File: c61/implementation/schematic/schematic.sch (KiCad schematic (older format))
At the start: 0 parts

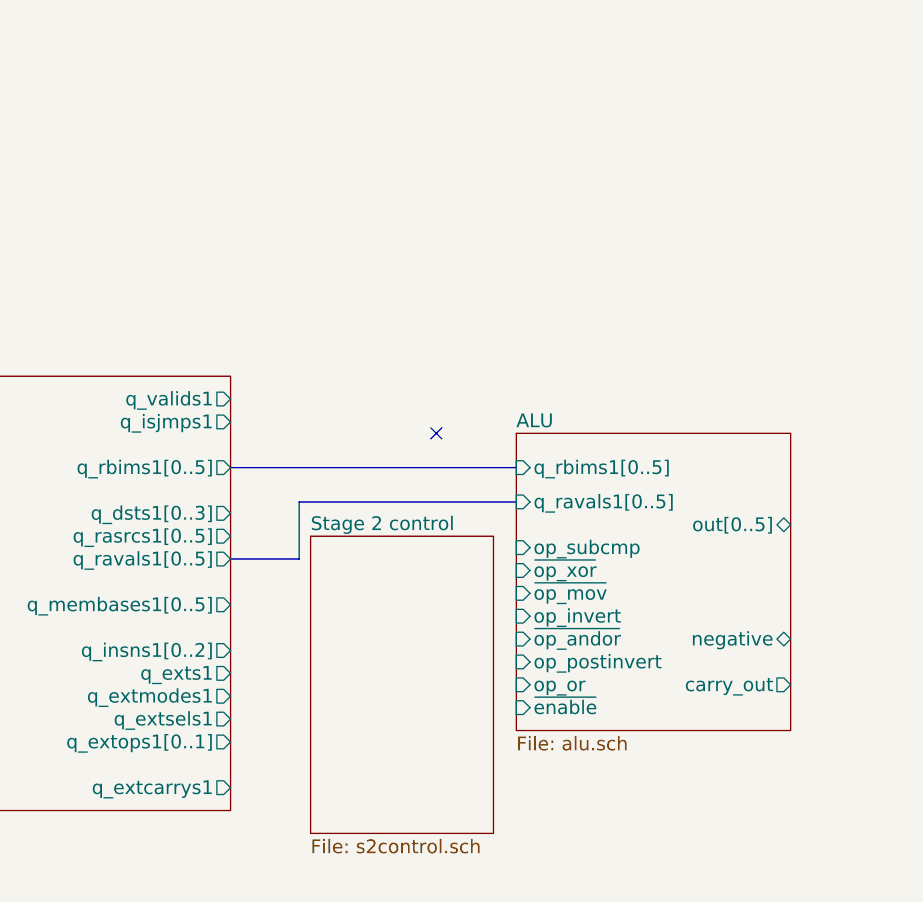
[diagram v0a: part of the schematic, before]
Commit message: C61: more updates to schematic
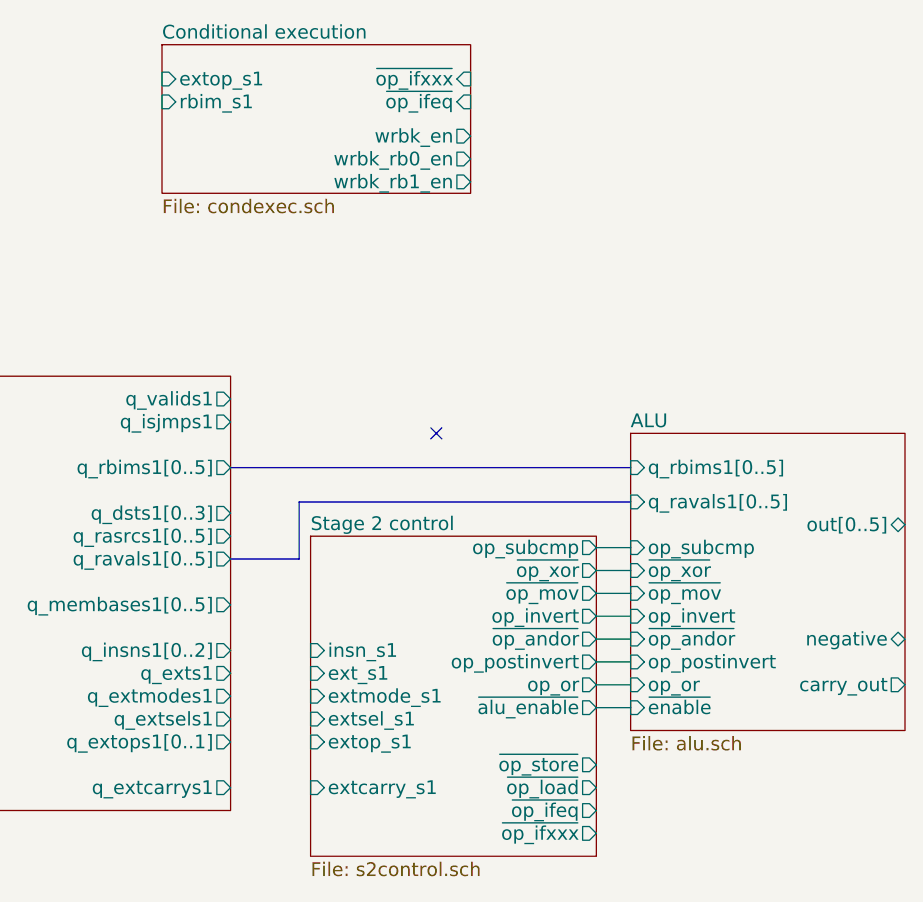
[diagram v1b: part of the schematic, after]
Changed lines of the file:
@@
 $Descr A4 11693 8268
 encoding utf-8
-Sheet 1 8
+Sheet 1 9
 Title ""
 Date ""
@@
 Connection ~ 2500 2350
 $Sheet
-S 9200 2500 1200 1300
+S 9700 2500 1200 1300
 U 5B67573A
 F0 "ALU" 60
 F1 "alu.sch" 60
-F2 "q_rbims1[0..5]" I L 9200 2650 60
-F3 "q_ravals1[0..5]" I L 9200 2800 60
-F4 "op_subcmp" I L 9200 3000 60
-F5 "~op_xor" I L 9200 3100 60
-F6 "~op_mov" I L 9200 3200 60
-F7 "op_invert" I L 9200 3300 60
-F8 "~op_andor" I L 9200 3400 60
-F9 "op_postinvert" I L 9200 3500 60
-F10 "op_or" I L 9200 3600 60
-F11 "~enable" I L 9200 3700 60
-F12 "out[0..5]" T R 10400 2900 60
-F13 "negative" T R 10400 3400 60
-F14 "carry_out" O R 10400 3600 60
-$EndSheet
-$Sheet
-S 8300 2950 800  1300
+F2 "q_rbims1[0..5]" I L 9700 2650 60
+F3 "q_ravals1[0..5]" I L 9700 2800 60
+F4 "op_subcmp" I L 9700 3000 60
+F5 "~op_xor" I L 9700 3100 60
+F6 "~op_mov" I L 9700 3200 60
+F7 "op_invert" I L 9700 3300 60
+F8 "~op_andor" I L 9700 3400 60
+F9 "op_postinvert" I L 9700 3500 60
+F10 "op_or" I L 9700 3600 60
+F11 "~enable" I L 9700 3700 60
+F12 "out[0..5]" T R 10900 2900 60
+F13 "negative" T R 10900 3400 60
+F14 "carry_out" O R 10900 3600 60
+$EndSheet
+$Sheet
+S 8300 2950 1250 1400
 U 5B6757FA
 F0 "Stage 2 control" 60
 F1 "s2control.sch" 60
+F2 "insn_s1" I L 8300 3450 60
+F3 "ext_s1" I L 8300 3550 60
+F4 "extmode_s1" I L 8300 3650 60
+F5 "extsel_s1" I L 8300 3750 60
+F6 "extop_s1" I L 8300 3850 60
+F7 "extcarry_s1" I L 8300 4050 60
+F8 "op_subcmp" O R 9550 3000 60
+F9 "~op_xor" O R 9550 3100 60
+F10 "~op_mov" O R 9550 3200 60
+F11 "~op_andor" O R 9550 3400 60
+F12 "op_invert" O R 9550 3300 60
+F13 "op_or" O R 9550 3600 60
+F14 "op_postinvert" O R 9550 3500 60
+F15 "~alu_enable" O R 9550 3700 60
+F16 "~op_store" O R 9550 3950 60
+F17 "~op_load" O R 9550 4050 60
+F18 "~op_ifeq" O R 9550 4150 60
+F19 "~op_ifxxx" O R 9550 4250 60
 $EndSheet
 Wire Bus Line
@@
 	8250 3050 8250 2800
 Wire Bus Line
-	8250 2800 9200 2800
-Wire Bus Line
-	7950 2650 9200 2650
+	8250 2800 9700 2800
+Wire Bus Line
+	7950 2650 9700 2650
 NoConn ~ 8850 2500
+Wire Wire Line
+	9550 3000 9700 3000
+Wire Wire Line
+	9550 3100 9700 3100
+Wire Wire Line
+	9550 3200 9700 3200
+Wire Wire Line
+	9550 3300 9700 3300
+Wire Wire Line
+	9550 3400 9700 3400
+Wire Wire Line
+	9550 3500 9700 3500
+Wire Wire Line
+	9550 3600 9700 3600
+Wire Wire Line
+	9550 3700 9700 3700
+$Sheet
+S 7650 800  1350 650
+U 5B95BAE6
+F0 "Conditional execution" 60
+F1 "condexec.sch" 60
+F2 "~op_ifeq" I R 9000 1050 60
+F3 "~op_ifxxx" I R 9000 950 60
+F4 "extop_s1" I L 7650 950 60
+F5 "rbim_s1" I L 7650 1050 60
+F6 "wrbk_en" O R 9000 1200 60
+F7 "wrbk_rb0_en" O R 9000 1300 60
+F8 "wrbk_rb1_en" O R 9000 1400 60
+$EndSheet
 $EndSCHEMATC
